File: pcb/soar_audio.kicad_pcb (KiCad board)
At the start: 4 copper layers, 79 x 51 mm, 113 parts, among them J1 RJ45-FLAPS, J10 HEADER_2, J11 HEADER_6, J2 RJ12-FLAPS, J3 HEADER_4, J4 Screw_Terminal_01x02, J5 RJ45-CAN, J6 HEADER_4, J7 HEADER_2, J8 HEADER_4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

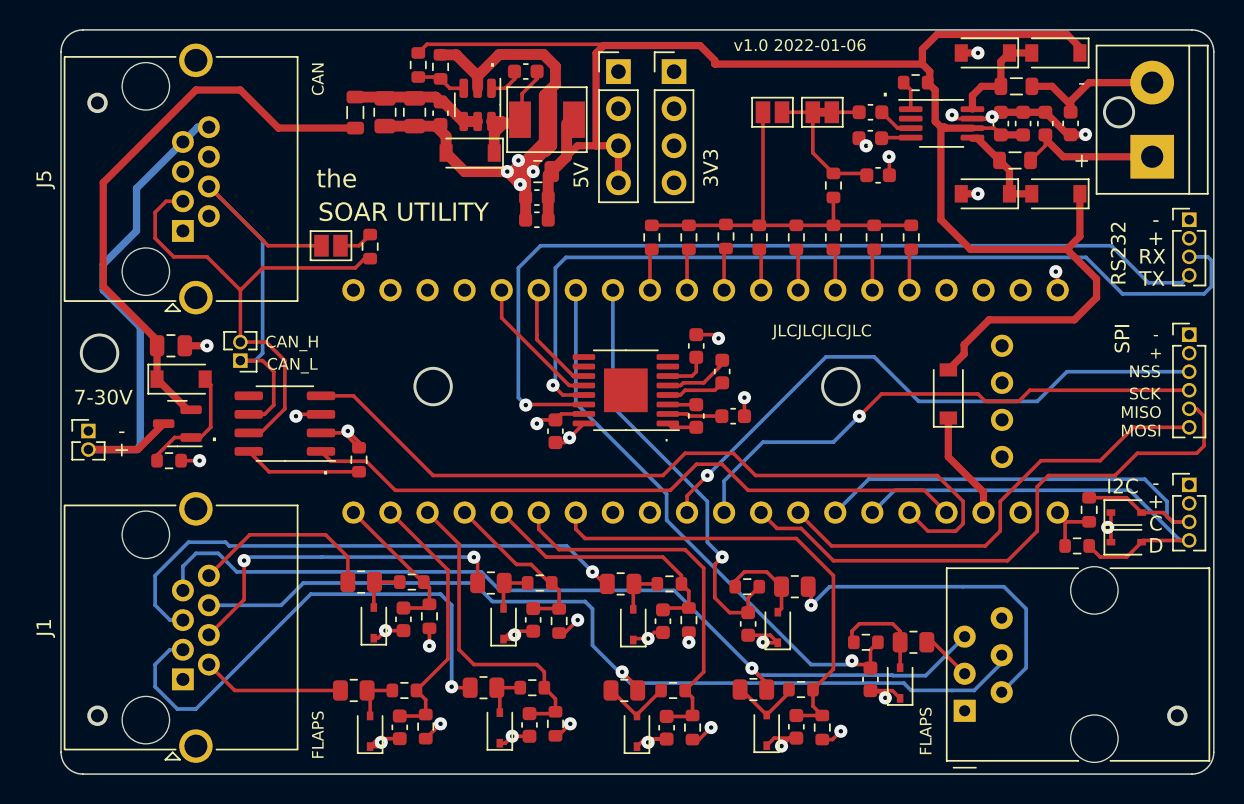
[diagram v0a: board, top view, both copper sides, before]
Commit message: changed dc-dc converter
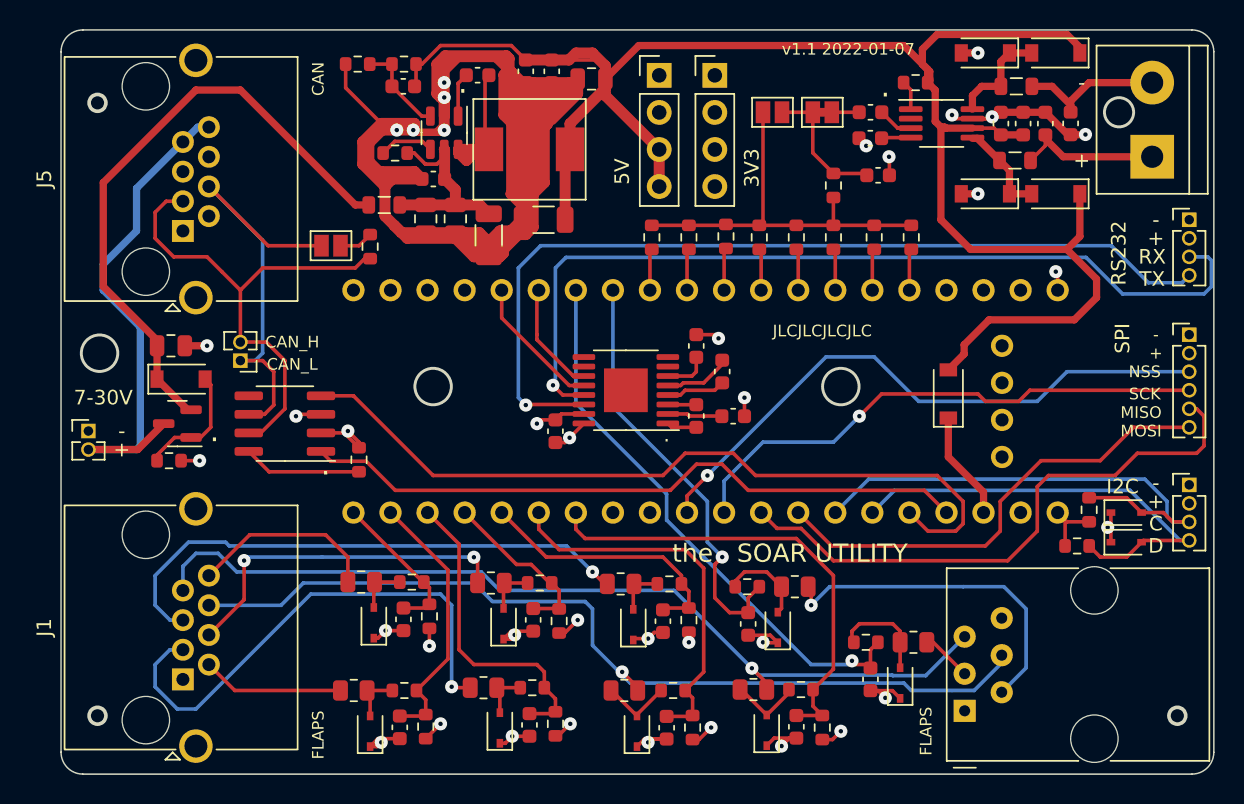
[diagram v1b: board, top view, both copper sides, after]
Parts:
- removed D3: D_B5819W, Diode_SMD:D_SOD-123
- added C30: 100p, Capacitor_SMD:C_0603_1608Metric, F.Cu at (125.0, 70.9)
- added C31: 47u, Capacitor_SMD:C_1206_3216Metric, F.Cu at (134.6, 80.0)
- added C32: 47u, Capacitor_SMD:C_1206_3216Metric, F.Cu at (130.8, 81.1)
- added R11: 100k, Resistor_SMD:R_0603_1608Metric, F.Cu at (124.4, 75.4)
- L1: value 10u -> 15u; footprint OWN_PARTS:MWSA0402S -> OWN_PARTS:SLO0630H
- R5: value 54k9 -> 105k
- R6: value 10k -> 20k
- U1: value LV2842X -> SCT2400
- moved C8 10.2 mm to (135.1, 69.8), turned to -90 degrees
- moved C2 8.75 mm to (128.5, 79.9)
- moved C10 8.68 mm to (133.3, 69.8), turned to 90 degrees
- moved C4 7.34 mm to (126.5, 79.9)
- moved C9 7.34 mm to (137.9, 70.4)
- moved FB1 6.63 mm to (123.7, 79.0), turned to 0 degrees
- moved R6 5.68 mm to (121.8, 69.3), turned to 180 degrees
- moved C3 4.53 mm to (127.0, 77.2), turned to 0 degrees
- moved C7 3.31 mm to (130.0, 70.1)
- moved U1 2.98 mm to (127.8, 74.0)
- moved J8 2.81 mm to (142.5, 70.1)
- moved J9 2.81 mm to (146.3, 70.1)
- moved L1 2.36 mm to (133.6, 75.2)
- moved R5 0.98 mm to (125.0, 69.3), turned to 180 degrees
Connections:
- U1 pad 4: Net-(C2-Pad1) -> Net-(U1-Pad4)
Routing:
- net GND: track 104.0 -> 221.2 mm, vias 27 -> 28
- net +5V: track 116.6 -> 128.2 mm
- net Net-(C2-Pad1): track 9.80 -> 17.9 mm
- net Net-(U1-Pad4): track 0.00 -> 3.80 mm
- net Net-(C7-Pad1): track 8.43 -> 12.1 mm
- net VSUPPLY: track 39.2 -> 42.3 mm
- net Net-(R6-Pad1): track 3.43 -> 6.53 mm
- net Net-(C7-Pad2): track 2.37 -> 3.04 mm
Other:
- board text added: "v1.1 2022-01-07"
- board text removed: "v1.0 2022-01-06"
